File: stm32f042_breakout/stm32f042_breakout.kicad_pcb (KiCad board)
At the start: 2 copper layers, 72 x 62 mm, 32 parts, among them J1 PGM, J10 MNT, J11 MNT, J12 MNT, J13 MNT, J2 USB_B_Micro, J3 PORTB, J4 PORTB, J5 POWER, J6 3.3v REG SW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

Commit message: bump design
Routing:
- net GND: track 453.3 -> 482.0 mm, vias 44 -> 50
- net ~RST~: track 67.8 -> 64.2 mm
- net CARD_DET: track 88.0 -> 89.3 mm
- net SPIMOSI: track 53.3 -> 54.5 mm
- net PB1: track 38.9 -> 38.0 mm

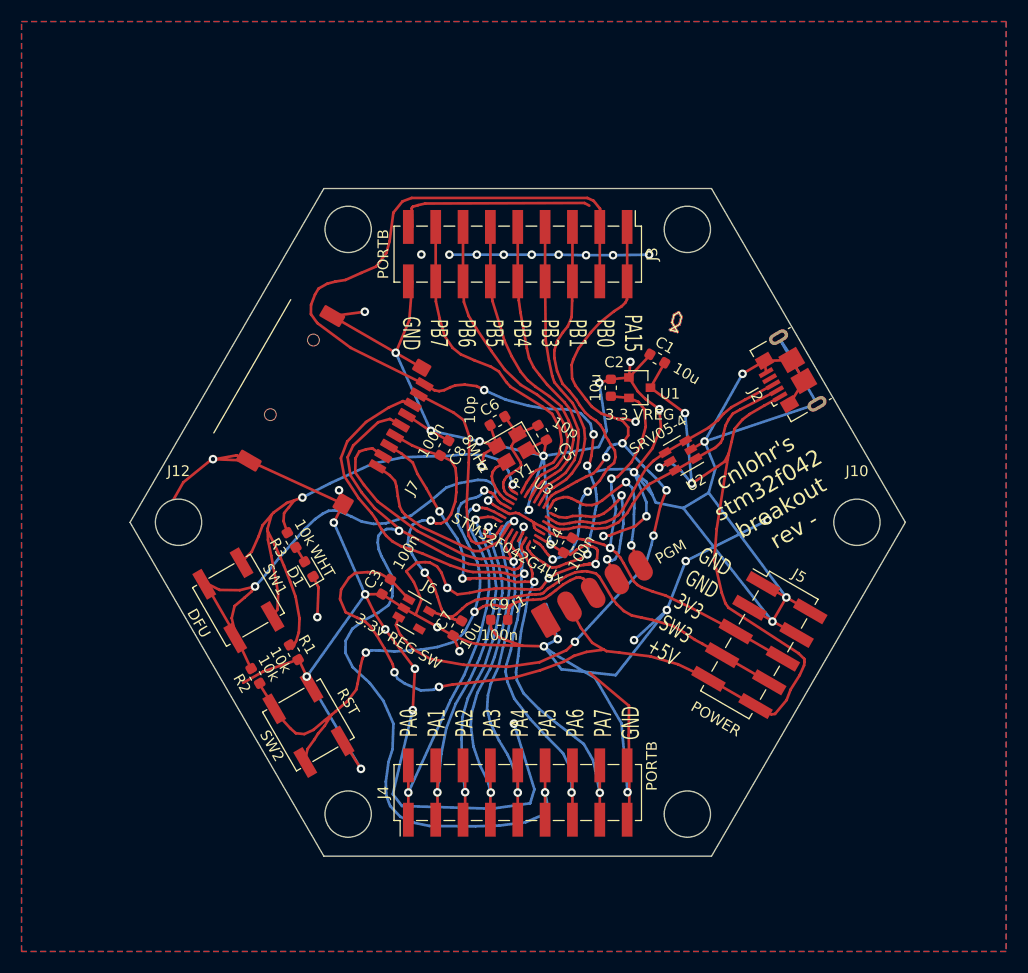
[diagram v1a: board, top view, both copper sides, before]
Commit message: Add the breakout, as printed.
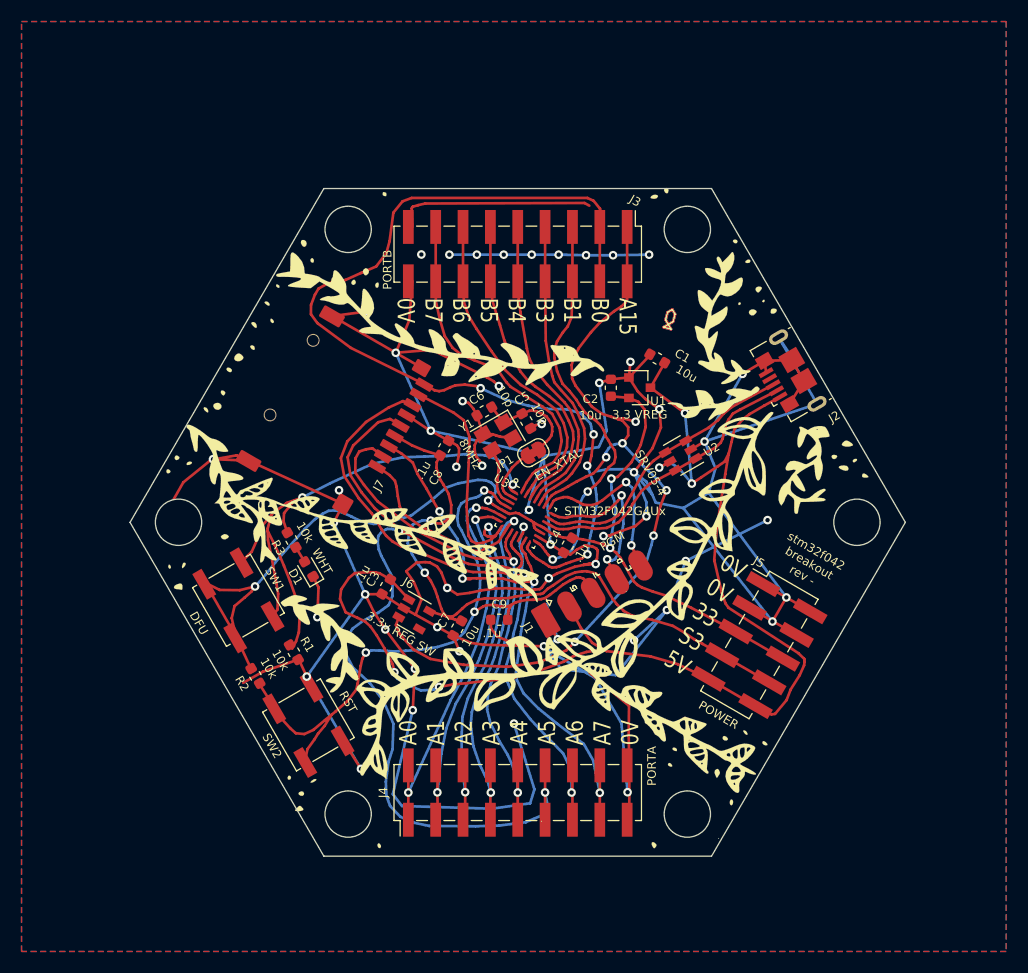
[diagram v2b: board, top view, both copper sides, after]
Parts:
- added J14: ARTWORK, stm32f042_breakout:back-artwork-cristabelle-braden-vsmall, B.Cu at (157.7, 77.3)
- added J15: ARTWORK, stm32f042_breakout:leaves_front-cristabelle, F.Cu at (168.2, 72.5)
- added J16: ARTWORK, stm32f042_breakout:cb-signature, B.Cu at (185.2, 95.5)
- added JP1: EN_XTAL, Jumper:SolderJumper-2_P1.3mm_Bridged_RoundedPad1.0x1.5mm, F.Cu at (169.4, 65.5)
- C3, C4, C8, C9: value 100n -> .1u
- J10, J11, J12, J13, J8, J9: footprint MountingHole:MountingHole_4.3mm_M4_DIN965 -> stm32f042_breakout:stm32f042_breakout_pin
- J4: value PORTB -> PORTA
- moved C5 1.83 mm to (168.8, 62.5)
- moved Y1 1.70 mm to (166.1, 63.9)
- moved C6 1.50 mm to (164.9, 61.6)
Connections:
- U3 pad 2: Net-(C5-Pad2) -> Net-(JP1-Pad2)
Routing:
- net GND: track 482.0 -> 495.1 mm, vias 50 -> 52
- net Net-(JP1-Pad2): track 0.00 -> 5.25 mm
- net Net-(C5-Pad2): track 11.5 -> 9.76 mm
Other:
- board text added: "0V 0V 33 S3 5V"
- board text added: "A0 A1 A2 A3 A4 A5 A6 A7 0V"
- board text added: "A15 B0 B1 B3 B4 B5 B6 B7 0V"
- board text added: "stm32f042 breakout rev -"
- board text removed: "GND GND 3V3 SW3 +5V"
- board text removed: "PA0 PA1 PA2 PA3 PA4 PA5 PA6 PA7 GND"
- board text removed: "PA15 PB0 PB1 PB3 PB4 PB5 PB6 PB7 GND"
- board text removed: "cnlohr's stm32f042 breakout rev -"
